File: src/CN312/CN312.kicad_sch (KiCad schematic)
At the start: 9 parts, among them J1 input, J2 output, Q1 NMOS, U1 CN312

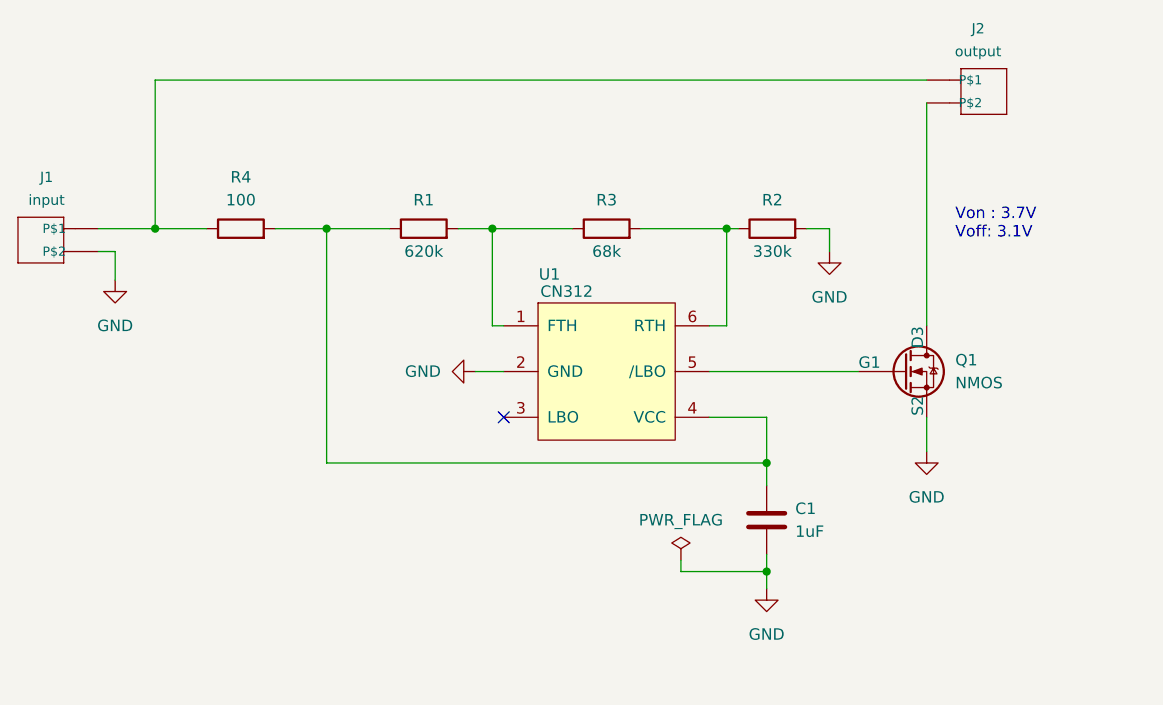
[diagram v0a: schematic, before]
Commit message: Add files via upload
PH2.0 的所在附近不要這麼大片的舖銅比較好，以防止意外造成短路。 (感謝周喬治大的貢獻)
Reduce copper pour area near PH2.0 to prevent accidental shorts. (Thanks to George Chou)
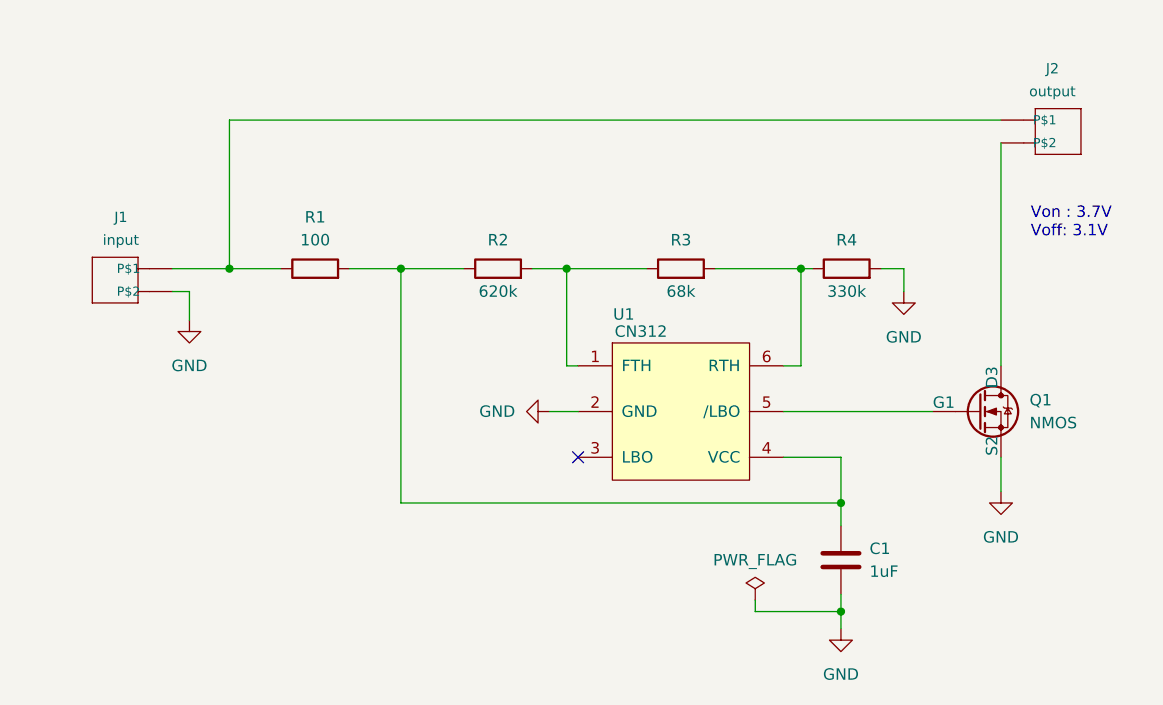
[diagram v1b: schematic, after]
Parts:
- renumbered R4 to R1, R1 to R2, R2 to R4
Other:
- moved on the sheet: C1, J1, J2, Q1, R1, R2, R3, R4, U1
